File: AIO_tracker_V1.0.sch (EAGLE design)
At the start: 75 parts, among them IC1 TPS61201, IC2 TPS61201, J1 EDGE_ICSP, Q1 MOSFET-PCHANNELSMD, U1 ATMEGA328P-AU, U2 USD-SOCKETNEW, X1 SMA-142-0701-881/886, Y1 ABRACON_ABM3_CRYSTAL

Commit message: Several thing corrected (still....=/)
Position of 9DOF, tended vias, names, etc
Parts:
- U$1: value UBLOX_MAX-6 -> UBLOX_MAX; device Ava:UBLOX_MAX-6 -> Ava:UBLOX_MAX
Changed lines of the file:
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@@
 <?xml version="1.0" encoding="utf-8"?>
 <!DOCTYPE eagle SYSTEM "eagle.dtd">
-<eagle version="6.4">
+<eagle version="6.5.0">
 <drawing>
 <settings>
@@
 </variantdefs>
 <classes>
-<class number="0" name="default" width="0.1524" drill="0.4">
-<clearance class="0" value="0.1524"/>
+<class number="0" name="default" width="0.254" drill="0.4">
+<clearance class="0" value="0.254"/>
 </class>
-<class number="1" name="bat" width="0.1524" drill="0.4">
-<clearance class="0" value="0.1524"/>
-<clearance class="1" value="0.1524"/>
+<class number="1" name="bat" width="0.254" drill="0.4">
+<clearance class="0" value="0.254"/>
+<clearance class="1" value="0.254"/>
 </class>
-<class number="2" name="5V" width="0.1524" drill="0.4">
-<clearance class="0" value="0.1524"/>
-<clearance class="1" value="0.1524"/>
-<clearance class="2" value="0.1524"/>
+<class number="2" name="5V" width="0.254" drill="0.4">
+<clearance class="0" value="0.254"/>
+<clearance class="1" value="0.254"/>
+<clearance class="2" value="0.254"/>
 </class>
-<class number="3" name="3.3V" width="0.1524" drill="0.4">
-<clearance class="0" value="0.1524"/>
-<clearance class="1" value="0.1524"/>
-<clearance class="2" value="0.1524"/>
-<clearance class="3" value="0.1524"/>
+<class number="3" name="3.3V" width="0.254" drill="0.4">
+<clearance class="0" value="0.254"/>
+<clearance class="1" value="0.254"/>
+<clearance class="2" value="0.254"/>
+<clearance class="3" value="0.254"/>
 </class>
-<class number="4" name="GND" width="0.1524" drill="0.4">
-<clearance class="0" value="0.1524"/>
-<clearance class="1" value="0.1524"/>
-<clearance class="2" value="0.1524"/>
-<clearance class="3" value="0.1524"/>
-<clearance class="4" value="0.1524"/>
+<class number="4" name="GND" width="0.254" drill="0.4">
+<clearance class="0" value="0.254"/>
+<clearance class="1" value="0.254"/>
+<clearance class="2" value="0.254"/>
+<clearance class="3" value="0.254"/>
+<clearance class="4" value="0.254"/>
 </class>
 </classes>
 <parts>
-<part name="U$1" library="Ava" deviceset="UBLOX_MAX-6" device=""/>
+<part name="U$1" library="Ava" deviceset="UBLOX_MAX" device=""/>
 <part name="U1" library="Ava" deviceset="ATMEGA328P-AU" device="" value=""/>
 <part name="U$3" library="Ava" deviceset="NTX2-VERTICAL" device=""/>

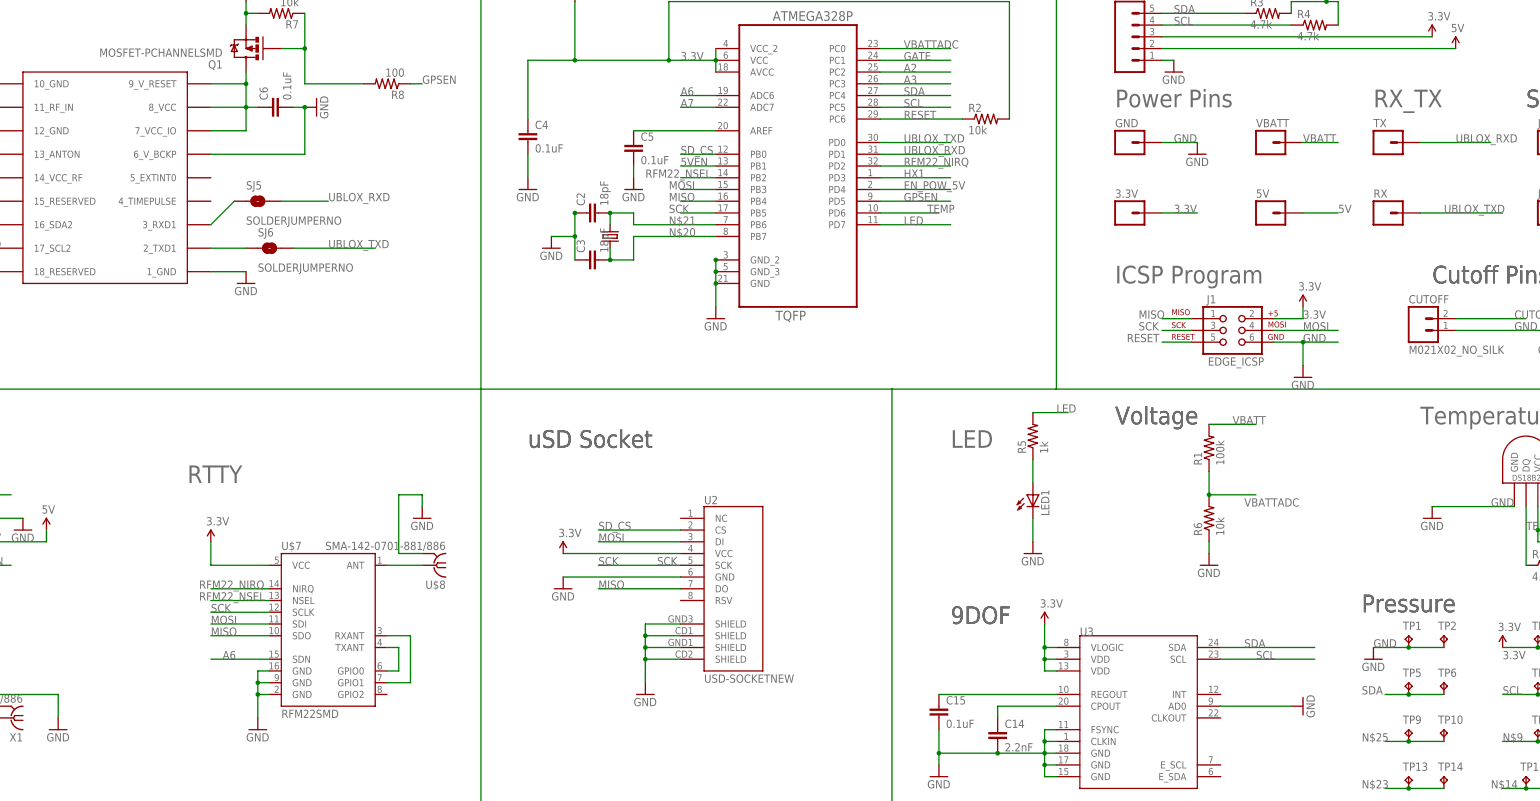
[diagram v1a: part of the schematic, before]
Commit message: fixed some details after receiving the printed pcb
- Fixed size of silkscreen
- Added pin 1 points in silkscreen
- Removed A6 and replaced the SDN of RFM22 with a 3way jumper

Still need to be fixed
- Pressure sensor size in pcb
- Buy the correct SMA Jacks (
http://pt.mouser.com/ProductDetail/Johnson-Cinch-Connectivity-Solutions/142-0701-881/?qs=sGAEpiMZZMuLQf%252bEuFsOrowCuZJUT8YljUsshXITPkY%3d)
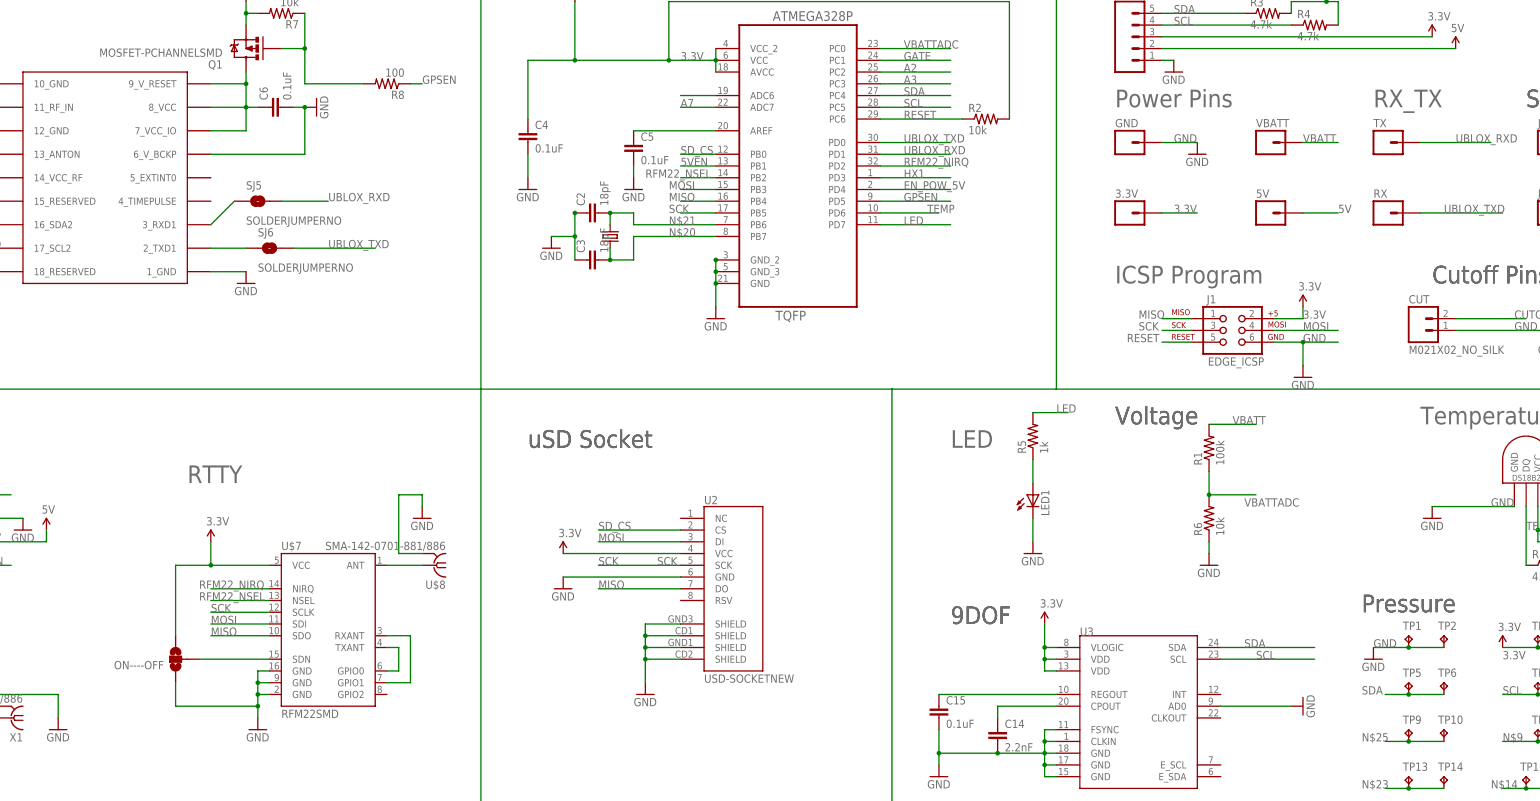
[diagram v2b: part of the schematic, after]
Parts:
- added ON----OFF: (no value), SparkFun-Passives:SOLDERJUMPER_2WAY-OLDT
- renumbered CUTOFF to CUT
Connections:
- removed net A6: U$7.SDN, U1.ADC6
- new net N$24: U1.ADC6
- new net N$26: ON----OFF.2, U$7.SDN
- net 3.3V: now also ON----OFF.3
- net GND: now also ON----OFF.1
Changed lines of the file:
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@@
 <part name="TP14" library="testpad" deviceset="TP" device="TP10SQ" value="TPTP10SQ"/>
 <part name="U$5" library="SparkFun-PowerIC" deviceset="LM2931_FIXED" device=""/>
-<part name="CUTOFF" library="SparkFun-Connectors" deviceset="M02" device="1X02_NO_SILK" value="M021X02_NO_SILK"/>
+<part name="CUT" library="SparkFun-Connectors" deviceset="M02" device="1X02_NO_SILK" value="M021X02_NO_SILK"/>
 <part name="GND26" library="SparkFun-Aesthetics" deviceset="GND" device=""/>
+<part name="ON----OFF" library="SparkFun-Passives" deviceset="SOLDERJUMPER_2WAY-OLD" device="T"/>
 </parts>
 <sheets>
@@
 <instance part="TP14" gate="G$1" x="243.84" y="-165.1"/>
 <instance part="U$5" gate="G$1" x="-73.66" y="48.26"/>
-<instance part="CUTOFF" gate="G$1" x="238.76" y="-68.58"/>
+<instance part="CUT" gate="G$1" x="238.76" y="-68.58"/>
 <instance part="GND26" gate="1" x="266.7" y="-71.12"/>
+<instance part="ON----OFF" gate="G$1" x="-30.48" y="-139.7" rot="R180"/>
 </instances>
 <busses>
@@
 <wire x1="-22.86" y1="-119.38" x2="-22.86" y2="-114.3" width="0.1524" layer="91"/>
 <pinref part="SUPPLY13" gate="G$1" pin="3.3V"/>
+<pinref part="ON----OFF" gate="G$1" pin="3"/>
+<wire x1="-30.48" y1="-134.62" x2="-30.48" y2="-119.38" width="0.1524" layer="91"/>
+<wire x1="-30.48" y1="-119.38" x2="-22.86" y2="-119.38" width="0.1524" layer="91"/>
+<junction x="-22.86" y="-119.38"/>
 </segment>
 <segment>
@@
 <pinref part="U$7" gate="G$1" pin="GND@1"/>
 <wire x1="-12.7" y1="-147.32" x2="-10.16" y2="-147.32" width="0.1524" layer="91"/>
-<wire x1="-12.7" y1="-152.4" x2="-12.7" y2="-147.32" width="0.1524" layer="91"/>
+<wire x1="-12.7" y1="-152.4" x2="-12.7" y2="-149.86" width="0.1524" layer="91"/>
 <junction x="-12.7" y="-144.78"/>
 <junction x="-12.7" y="-147.32"/>
 <pinref part="GND23" gate="1" pin="GND"/>
+<pinref part="ON----OFF" gate="G$1" pin="1"/>
+<wire x1="-12.7" y1="-149.86" x2="-12.7" y2="-147.32" width="0.1524" layer="91"/>
+<wire x1="-30.48" y1="-144.78" x2="-30.48" y2="-149.86" width="0.1524" layer="91"/>
+<wire x1="-30.48" y1="-149.86" x2="-12.7" y2="-149.86" width="0.1524" layer="91"/>
+<junction x="-12.7" y="-149.86"/>
 </segment>
 <segment>
@@
 </segment>
 <segment>
-<pinref part="CUTOFF" gate="G$1" pin="1"/>
+<pinref part="CUT" gate="G$1" pin="1"/>
 <wire x1="246.38" y1="-68.58" x2="266.7" y2="-68.58" width="0.1524" layer="91"/>
 <pinref part="GND26" gate="1" pin="GND"/>
@@
 </segment>
 </net>
-<net name="A6" class="0">
-<segment>
-<pinref part="U1" gate="A" pin="ADC6"/>
-<wire x1="86.36" y1="-17.78" x2="78.74" y2="-17.78" width="0.1524" layer="91"/>
-<label x="78.74" y="-17.78" size="1.778" layer="95"/>
-</segment>
-<segment>
-<pinref part="U$7" gate="G$1" pin="SDN"/>
-<wire x1="-10.16" y1="-139.7" x2="-22.86" y2="-139.7" width="0.1524" layer="91"/>
-<label x="-20.32" y="-139.7" size="1.778" layer="95"/>
-</segment>
-</net>
 <net name="N$17" class="0">
 <segment>
@@
 </segment>
 <segment>
-<pinref part="CUTOFF" gate="G$1" pin="2"/>
+<pinref part="CUT" gate="G$1" pin="2"/>
 <wire x1="246.38" y1="-66.04" x2="261.62" y2="-66.04" width="0.1524" layer="91"/>
 <label x="259.08" y="-66.04" size="1.778" layer="95"/>
@@
 </segment>
 </net>
+<net name="N$24" class="0">
+<segment>
+<pinref part="U1" gate="A" pin="ADC6"/>
+<wire x1="86.36" y1="-17.78" x2="78.74" y2="-17.78" width="0.1524" layer="91"/>
+</segment>
+</net>
+<net name="N$26" class="0">
+<segment>
+<pinref part="U$7" gate="G$1" pin="SDN"/>
+<pinref part="ON----OFF" gate="G$1" pin="2"/>
+<wire x1="-10.16" y1="-139.7" x2="-25.4" y2="-139.7" width="0.1524" layer="91"/>
+</segment>
+</net>

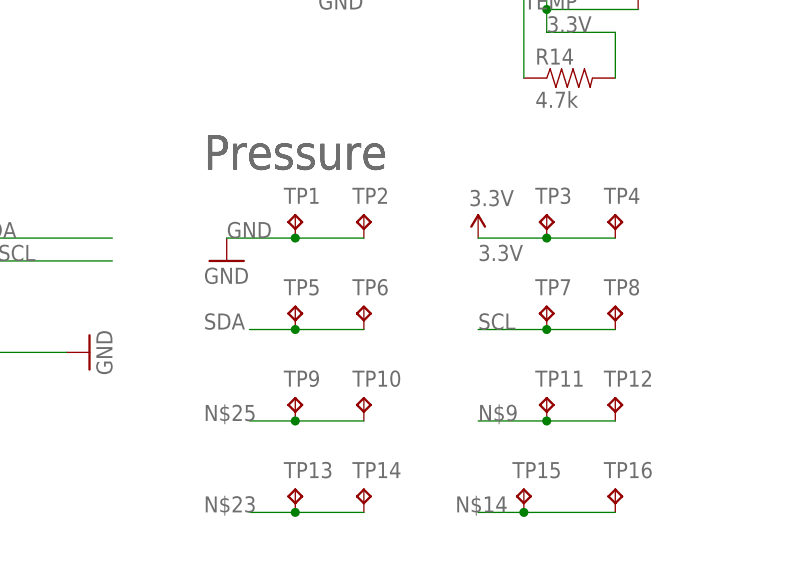
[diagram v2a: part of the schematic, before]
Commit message: last changes post fabrication
- changed position of the pressure sensor pins (reversed)
- Added more spacing from the AA battery holders
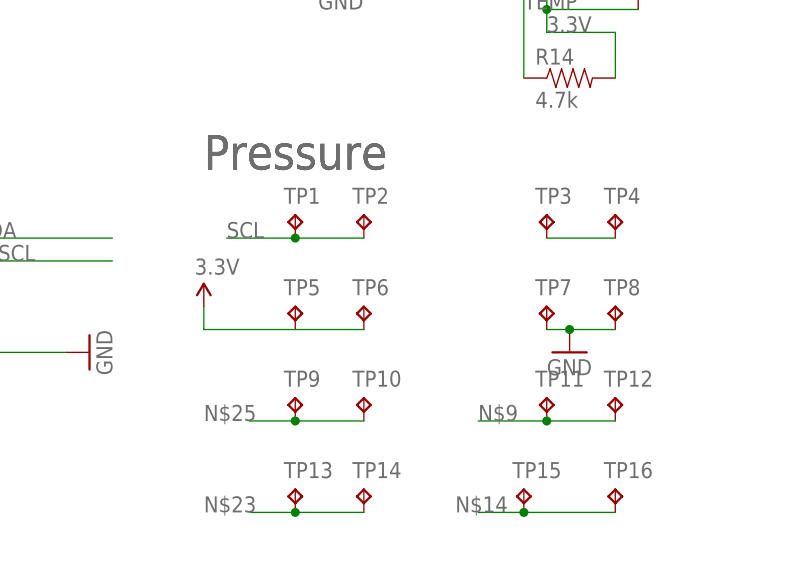
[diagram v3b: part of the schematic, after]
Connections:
- net 3.3V: now also TP5.TP, TP6.TP; no longer TP3.TP, TP4.TP
- net GND: now also TP7.TP, TP8.TP; no longer TP1.TP, TP2.TP
- net SCL: now also TP1.TP, TP2.TP; no longer TP7.TP, TP8.TP
- net SDA: now also TP3.TP, TP4.TP; no longer TP5.TP, TP6.TP
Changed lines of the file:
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@@
 <part name="TP15" library="testpad" deviceset="TP" device="TP10SQ" value="TPTP10SQ"/>
 <part name="TP16" library="testpad" deviceset="TP" device="TP10SQ" value="TPTP10SQ"/>
-<part name="SUPPLY5" library="SparkFun-Aesthetics" deviceset="3.3V" device=""/>
-<part name="GND30" library="SparkFun-Aesthetics" deviceset="GND" device=""/>
 <part name="TP9" library="testpad" deviceset="TP" device="TP10SQ" value="TPTP10SQ"/>
 <part name="TP10" library="testpad" deviceset="TP" device="TP10SQ" value="TPTP10SQ"/>
@@
 <part name="GND26" library="SparkFun-Aesthetics" deviceset="GND" device=""/>
 <part name="ON----OFF" library="SparkFun-Passives" deviceset="SOLDERJUMPER_2WAY-OLD" device="T"/>
+<part name="GND30" library="SparkFun-Aesthetics" deviceset="GND" device=""/>
+<part name="SUPPLY6" library="SparkFun-Aesthetics" deviceset="3.3V" device=""/>
 </parts>
 <sheets>
@@
 <instance part="TP15" gate="G$1" x="261.62" y="-165.1"/>
 <instance part="TP16" gate="G$1" x="271.78" y="-165.1"/>
-<instance part="SUPPLY5" gate="G$1" x="256.54" y="-137.16"/>
-<instance part="GND30" gate="1" x="228.6" y="-139.7"/>
 <instance part="TP9" gate="G$1" x="236.22" y="-154.94"/>
 <instance part="TP10" gate="G$1" x="243.84" y="-154.94"/>
@@
 <instance part="GND26" gate="1" x="266.7" y="-71.12"/>
 <instance part="ON----OFF" gate="G$1" x="-30.48" y="-139.7" rot="R180"/>
+<instance part="GND30" gate="1" x="266.7" y="-149.86"/>
+<instance part="SUPPLY6" gate="G$1" x="226.06" y="-144.78"/>
 </instances>
 <busses>
@@
 </segment>
 <segment>
-<pinref part="TP4" gate="G$1" pin="TP"/>
-<pinref part="TP3" gate="G$1" pin="TP"/>
-<wire x1="271.78" y1="-137.16" x2="264.16" y2="-137.16" width="0.1524" layer="91"/>
-<wire x1="264.16" y1="-137.16" x2="256.54" y2="-137.16" width="0.1524" layer="91"/>
-<label x="256.54" y="-139.7" size="1.778" layer="95"/>
-<pinref part="SUPPLY5" gate="G$1" pin="3.3V"/>
-<junction x="264.16" y="-137.16"/>
+<pinref part="TP6" gate="G$1" pin="TP"/>
+<pinref part="TP5" gate="G$1" pin="TP"/>
+<wire x1="243.84" y1="-147.32" x2="236.22" y2="-147.32" width="0.1524" layer="91"/>
+<pinref part="SUPPLY6" gate="G$1" pin="3.3V"/>
+<wire x1="236.22" y1="-147.32" x2="226.06" y2="-147.32" width="0.1524" layer="91"/>
+<wire x1="226.06" y1="-147.32" x2="226.06" y2="-144.78" width="0.1524" layer="91"/>
 </segment>
 </net>
@@
 </segment>
 <segment>
-<pinref part="TP2" gate="G$1" pin="TP"/>
-<pinref part="TP1" gate="G$1" pin="TP"/>
-<wire x1="243.84" y1="-137.16" x2="236.22" y2="-137.16" width="0.1524" layer="91"/>
-<wire x1="236.22" y1="-137.16" x2="228.6" y2="-137.16" width="0.1524" layer="91"/>
-<label x="228.6" y="-137.16" size="1.778" layer="95"/>
-<pinref part="GND30" gate="1" pin="GND"/>
-<junction x="236.22" y="-137.16"/>
-</segment>
-<segment>
 <pinref part="CUT" gate="G$1" pin="1"/>
 <wire x1="246.38" y1="-68.58" x2="266.7" y2="-68.58" width="0.1524" layer="91"/>
 <pinref part="GND26" gate="1" pin="GND"/>
 <label x="259.08" y="-68.58" size="1.778" layer="95"/>
+</segment>
+<segment>
+<pinref part="TP8" gate="G$1" pin="TP"/>
+<pinref part="TP7" gate="G$1" pin="TP"/>
+<wire x1="271.78" y1="-147.32" x2="266.7" y2="-147.32" width="0.1524" layer="91"/>
+<pinref part="GND30" gate="1" pin="GND"/>
+<wire x1="266.7" y1="-147.32" x2="264.16" y2="-147.32" width="0.1524" layer="91"/>
+<junction x="266.7" y="-147.32"/>
 </segment>
 </net>
@@
 </segment>
 <segment>
-<pinref part="TP6" gate="G$1" pin="TP"/>
-<pinref part="TP5" gate="G$1" pin="TP"/>
-<wire x1="243.84" y1="-147.32" x2="236.22" y2="-147.32" width="0.1524" layer="91"/>
-<wire x1="236.22" y1="-147.32" x2="231.14" y2="-147.32" width="0.1524" layer="91"/>
-<label x="226.06" y="-147.32" size="1.778" layer="95"/>
-<junction x="236.22" y="-147.32"/>
+<pinref part="TP4" gate="G$1" pin="TP"/>
+<pinref part="TP3" gate="G$1" pin="TP"/>
+<wire x1="271.78" y1="-137.16" x2="264.16" y2="-137.16" width="0.1524" layer="91"/>
 </segment>
 </net>
@@
 </segment>
 <segment>
-<pinref part="TP8" gate="G$1" pin="TP"/>
-<pinref part="TP7" gate="G$1" pin="TP"/>
-<wire x1="271.78" y1="-147.32" x2="264.16" y2="-147.32" width="0.1524" layer="91"/>
-<wire x1="264.16" y1="-147.32" x2="256.54" y2="-147.32" width="0.1524" layer="91"/>
-<label x="256.54" y="-147.32" size="1.778" layer="95"/>
-<junction x="264.16" y="-147.32"/>
-</segment>
-</net>
+<pinref part="TP2" gate="G$1" pin="TP"/>
+<pinref part="TP1" gate="G$1" pin="TP"/>
+<wire x1="243.84" y1="-137.16" x2="236.22" y2="-137.16" width="0.1524" layer="91"/>
+<wire x1="236.22" y1="-137.16" x2="228.6" y2="-137.16" width="0.1524" layer="91"/>
+<label x="228.6" y="-137.16" size="1.778" layer="95"/>
+<junction x="236.22" y="-137.16"/>
+</segment>
+</net>
